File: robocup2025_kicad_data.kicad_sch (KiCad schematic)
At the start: 12 parts, among them U1 RASPBERRY_PI_4B_4GB, U2 ESP32-DEVKITC-32E

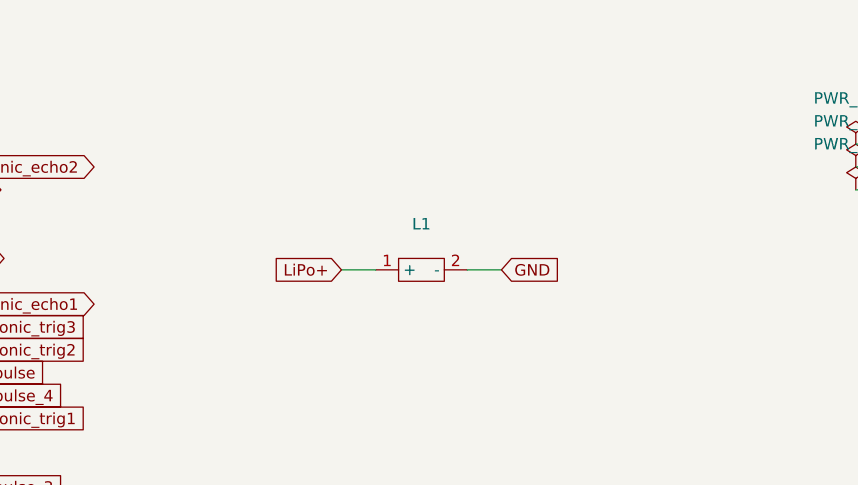
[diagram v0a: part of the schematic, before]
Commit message: robocup2025_kicad_data.kicad_sch: Added voltmeter in schematics
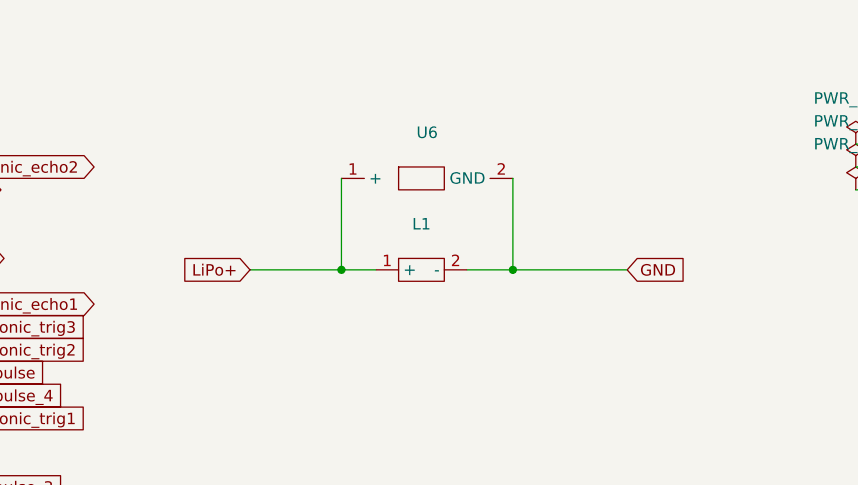
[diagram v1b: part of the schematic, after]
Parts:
- added U6: ~, symbol robo:voltmeter
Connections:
- net GND: now also U6.2 (GND)
- net LiPo+: now also U6.1 (+)
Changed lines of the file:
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@@
 	(generator_version "9.0")
 	(paper "A4")
+	(junction
+		(at 194.31 52.07)
+		(diameter 0)
+		(color 0 0 0 0)
+	)
+	(junction
+		(at 213.36 52.07)
+		(diameter 0)
+		(color 0 0 0 0)
+	)
 	(no_connect
 		(at 80.01 66.04)
@@
 	(wire
 		(pts
+			(xy 213.36 52.07) (xy 226.06 52.07)
+		)
+		(stroke
+			(width 0)
+			(type default)
+		)
+	)
+	(wire
+		(pts
 			(xy 146.05 63.5) (xy 149.86 63.5)
 		)
@@
 	(wire
 		(pts
-			(xy 208.28 52.07) (xy 212.09 52.07)
+			(xy 213.36 41.91) (xy 213.36 52.07)
+		)
+		(stroke
+			(width 0)
+			(type default)
+		)
+	)
+	(wire
+		(pts
+			(xy 208.28 52.07) (xy 213.36 52.07)
 		)
 		(stroke
@@
 	(wire
 		(pts
+			(xy 194.31 41.91) (xy 194.31 52.07)
+		)
+		(stroke
+			(width 0)
+			(type default)
+		)
+	)
+	(wire
+		(pts
+			(xy 184.15 52.07) (xy 194.31 52.07)
+		)
+		(stroke
+			(width 0)
+			(type default)
+		)
+	)
+	(wire
+		(pts
+			(xy 135.89 120.65) (xy 135.89 124.46)
+		)
+		(stroke
+			(width 0)
+			(type default)
+		)
+	)
+	(wire
+		(pts
+			(xy 74.93 121.92) (xy 74.93 125.73)
+		)
+		(stroke
+			(width 0)
+			(type default)
+		)
+	)
+	(wire
+		(pts
+			(xy 146.05 68.58) (xy 149.86 68.58)
+		)
+		(stroke
+			(width 0)
+			(type default)
+		)
+	)
+	(wire
+		(pts
+			(xy 101.6 73.66) (xy 105.41 73.66)
+		)
+		(stroke
+			(width 0)
+			(type default)
+		)
+	)
+	(wire
+		(pts
+			(xy 101.6 58.42) (xy 105.41 58.42)
+		)
+		(stroke
+			(width 0)
+			(type default)
+		)
+	)
+	(wire
+		(pts
+			(xy 146.05 76.2) (xy 149.86 76.2)
+		)
+		(stroke
+			(width 0)
+			(type default)
+		)
+	)
+	(wire
+		(pts
+			(xy 146.05 66.04) (xy 149.86 66.04)
+		)
+		(stroke
+			(width 0)
+			(type default)
+		)
+	)
+	(wire
+		(pts
+			(xy 130.81 120.65) (xy 130.81 124.46)
+		)
+		(stroke
+			(width 0)
+			(type default)
+		)
+	)
+	(wire
+		(pts
 			(xy 194.31 52.07) (xy 198.12 52.07)
 		)
@@
 	(wire
 		(pts
-			(xy 135.89 120.65) (xy 135.89 124.46)
-		)
-		(stroke
-			(width 0)
-			(type default)
-		)
-	)
-	(wire
-		(pts
-			(xy 74.93 121.92) (xy 74.93 125.73)
-		)
-		(stroke
-			(width 0)
-			(type default)
-		)
-	)
-	(wire
-		(pts
-			(xy 146.05 68.58) (xy 149.86 68.58)
-		)
-		(stroke
-			(width 0)
-			(type default)
-		)
-	)
-	(wire
-		(pts
-			(xy 101.6 73.66) (xy 105.41 73.66)
-		)
-		(stroke
-			(width 0)
-			(type default)
-		)
-	)
-	(wire
-		(pts
-			(xy 101.6 58.42) (xy 105.41 58.42)
-		)
-		(stroke
-			(width 0)
-			(type default)
-		)
-	)
-	(wire
-		(pts
-			(xy 146.05 76.2) (xy 149.86 76.2)
-		)
-		(stroke
-			(width 0)
-			(type default)
-		)
-	)
-	(wire
-		(pts
-			(xy 146.05 66.04) (xy 149.86 66.04)
-		)
-		(stroke
-			(width 0)
-			(type default)
-		)
-	)
-	(wire
-		(pts
-			(xy 130.81 120.65) (xy 130.81 124.46)
-		)
-		(stroke
-			(width 0)
-			(type default)
-		)
-	)
-	(wire
-		(pts
 			(xy 132.08 120.65) (xy 132.08 124.46)
 		)
@@
 	(global_label "GND"
 		(shape input)
-		(at 212.09 52.07 0)
+		(at 226.06 52.07 0)
 		(fields_autoplaced yes)
 		(effects
@@
 		)
 		(property "Intersheetrefs" "${INTERSHEET_REFS}"
-			(at 218.9457 52.07 0)
+			(at 232.9157 52.07 0)
 			(effects
 				(font
@@
 	(global_label "LiPo+"
 		(shape input)
-		(at 194.31 52.07 180)
-		(fields_autoplaced yes)
-		(effects
-			(font
-				(size 1.27 1.27)
-			)
-			(justify right)
-		)
-		(property "Intersheetrefs" "${INTERSHEET_REFS}"
-			(at 185.7005 52.07 0)
+		(at 184.15 52.07 180)
+		(fields_autoplaced yes)
+		(effects
+			(font
+				(size 1.27 1.27)
+			)
+			(justify right)
+		)
+		(property "Intersheetrefs" "${INTERSHEET_REFS}"
+			(at 175.5405 52.07 0)
 			(effects
 				(font
@@
 					(unit 1)
 				)
+			)
+		)
+	)
+	(symbol
+		(lib_id "robo:voltmeter")
+		(at 203.2 41.91 0)
+		(unit 1)
+		(exclude_from_sim no)
+		(in_bom yes)
+		(on_board yes)
+		(dnp no)
+		(fields_autoplaced yes)
+		(property "Reference" "U6"
+			(at 203.835 36.83 0)
+			(effects
+				(font
+					(size 1.27 1.27)
+				)
+			)
+		)
+		(property "Value" "~"
+			(at 203.835 39.37 0)
+			(effects
+				(font
+					(size 1.27 1.27)
+				)
+			)
+		)
+		(property "Footprint" ""
+			(at 203.2 41.91 0)
+			(effects
+				(font
+					(size 1.27 1.27)
+				)
+				(hide yes)
+			)
+		)
+		(property "Datasheet" ""
+			(at 203.2 41.91 0)
+			(effects
+				(font
+					(size 1.27 1.27)
+				)
+				(hide yes)
+			)
+		)
+		(property "Description" ""
+			(at 203.2 41.91 0)
+			(effects
+				(font
+					(size 1.27 1.27)
+				)
+				(hide yes)
+			)
+		)
+		(pin "2"
+		)
+		(pin "1"
+		)
+		(instances
+			(project ""
+				(path "/c41ae4e6-c818-4751-9662-d6273ae109e5"
+					(reference "U6")
+					(unit 1)
+				)

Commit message: robocup2025_kicad_data.kicad_sch: Assigned footprint for voltmeter
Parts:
- U6: footprint (none) -> robo:voltmeter
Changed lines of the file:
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@@
 			)
 		)
-		(property "Footprint" ""
+		(property "Footprint" "robo:voltmeter"
 			(at 203.2 41.91 0)
 			(effects

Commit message: robocup2025_kicad_data.kicad_sch: Remaped servo motor's footprints correctly
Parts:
- M1, M2, M3, M4, M5: footprint robo:servo_motor -> robo:servo_motor_4
- M6: footprint (none) -> robo:servo_motor_3
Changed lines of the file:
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@@
 			)
 		)
-		(property "Footprint" "robo:servo_motor"
+		(property "Footprint" "robo:servo_motor_4"
 			(at 54.61 118.11 0)
 			(effects
@@
 			)
 		)
-		(property "Footprint" "robo:servo_motor"
+		(property "Footprint" "robo:servo_motor_4"
 			(at 66.04 118.11 0)
 			(effects
@@
 			)
 		)
-		(property "Footprint" ""
+		(property "Footprint" "robo:servo_motor_3"
 			(at 148.59 120.65 0)
 			(effects
@@
 			)
 		)
-		(property "Footprint" "robo:servo_motor"
+		(property "Footprint" "robo:servo_motor_4"
 			(at 77.47 118.11 0)
 			(effects
@@
 			)
 		)
-		(property "Footprint" "robo:servo_motor"
+		(property "Footprint" "robo:servo_motor_4"
 			(at 88.9 118.11 0)
 			(effects
@@
 			)
 		)
-		(property "Footprint" "robo:servo_motor"
+		(property "Footprint" "robo:servo_motor_4"
 			(at 41.91 118.11 0)
 			(effects

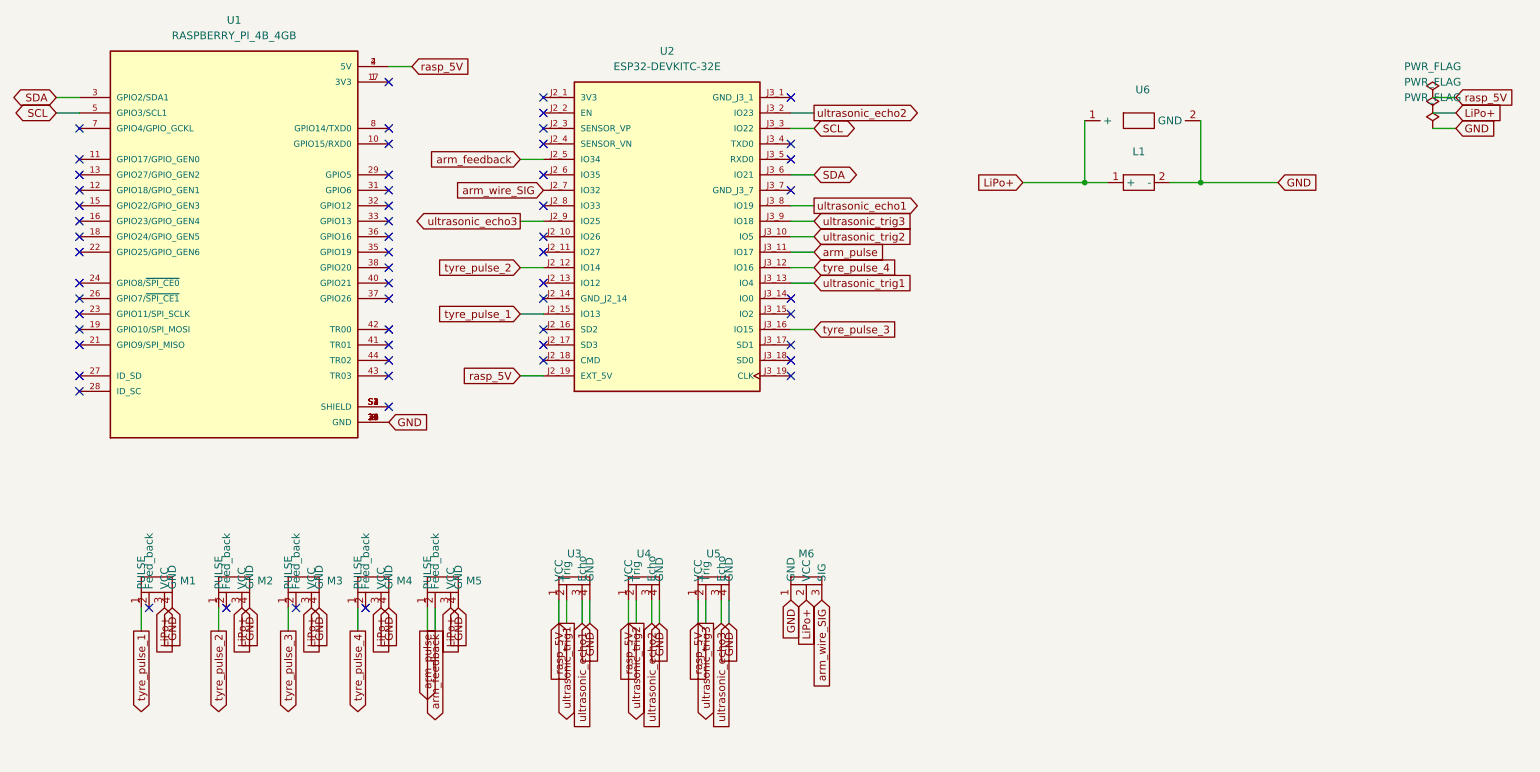
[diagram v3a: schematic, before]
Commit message: robocup2025_kicad_data.kicad_sch: Modified GND to use default symbol
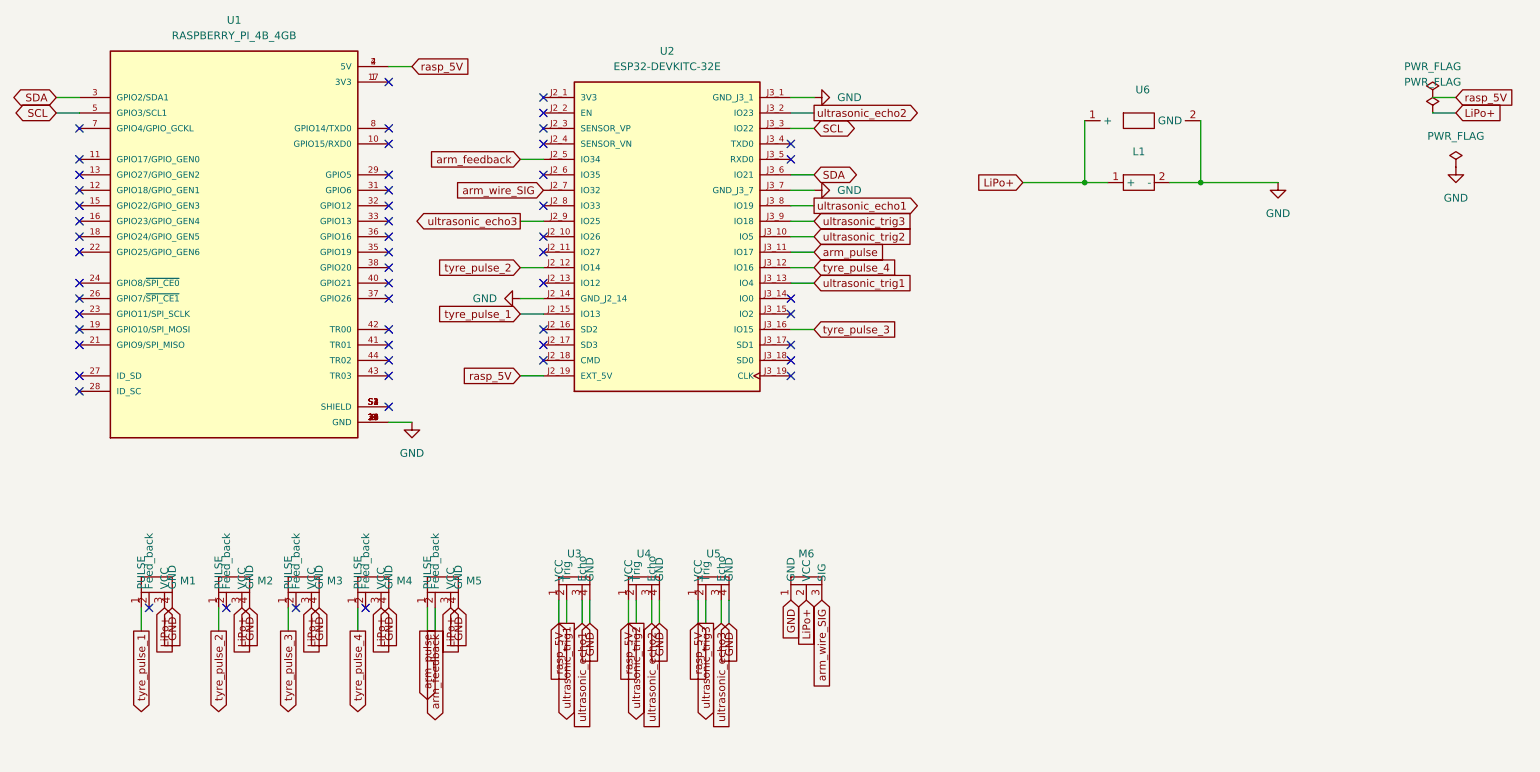
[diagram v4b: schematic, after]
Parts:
- U6: footprint robo:voltmeter -> (none)
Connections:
- net GND: now also U2.J2_14 (GND_J2_14), U2.J3_1 (GND_J3_1), U2.J3_7 (GND_J3_7)
- no-connect marks 58 -> 55

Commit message: robocup2025_kicad_data.kicad_sch: Applied footprint for voltmeter
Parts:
- U6: footprint (none) -> robo:voltmeter
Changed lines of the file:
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@@
 			)
 		)
-		(property "Footprint" ""
+		(property "Footprint" "robo:voltmeter"
 			(at 203.2 41.91 0)
 			(effects

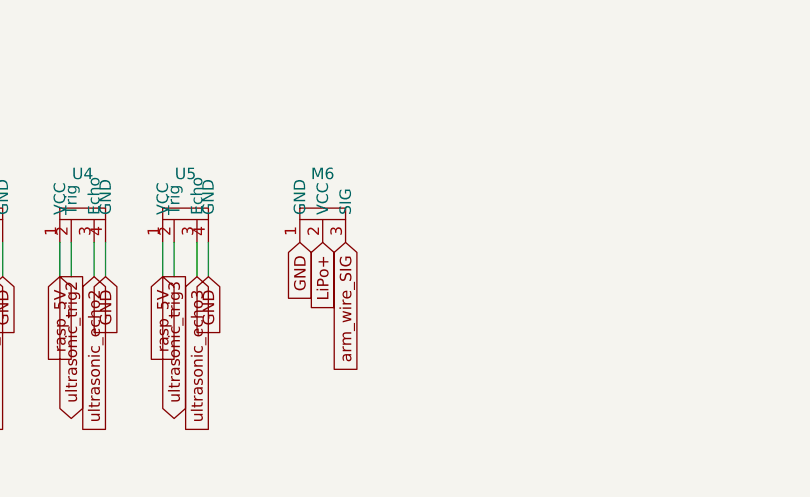
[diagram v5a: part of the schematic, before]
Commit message: robocup2025_kicad_data.kicad_sch: Changed to use default sch for simple servo
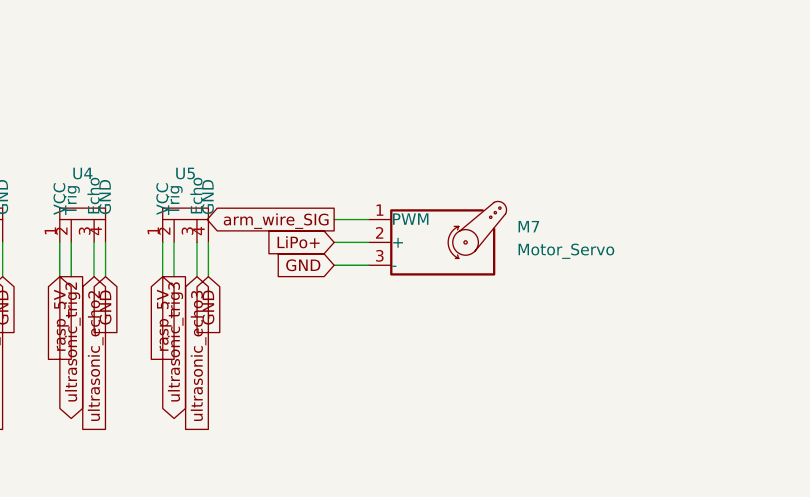
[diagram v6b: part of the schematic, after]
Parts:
- removed M6: ~, robo:servo_motor_3, symbol robo:arm_servo
- added M7: Motor_Servo, symbol Motor:Motor_Servo
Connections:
- net GND: now also M7.3 (-)
- net LiPo+: now also M7.2 (+)
- net arm_wire_SIG: now also M7.1 (PWM)
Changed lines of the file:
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@@
+	(wire
+		(pts
+			(xy 149.86 123.19) (xy 153.67 123.19)
+		)
+		(stroke
+			(width 0)
+			(type default)
+		)
+	)
 	(wire
 		(pts
@@
 	(wire
 		(pts
+			(xy 149.86 118.11) (xy 153.67 118.11)
+		)
+		(stroke
+			(width 0)
+			(type default)
+		)
+	)
+	(wire
+		(pts
 			(xy 194.31 41.91) (xy 194.31 52.07)
 		)
@@
 	(wire
 		(pts
+			(xy 149.86 120.65) (xy 153.67 120.65)
+		)
+		(stroke
+			(width 0)
+			(type default)
+		)
+	)
+	(wire
+		(pts
 			(xy 146.05 66.04) (xy 149.86 66.04)
 		)
@@
 		)
 	)
+	(global_label "LiPo+"
+		(shape input)
+		(at 149.86 120.65 180)
+		(fields_autoplaced yes)
+		(effects
+			(font
+				(size 1.27 1.27)
+			)
+			(justify right)
+		)
+		(property "Intersheetrefs" "${INTERSHEET_REFS}"
+			(at 141.2505 120.65 0)
+			(effects
+				(font
+					(size 1.27 1.27)
+				)
+				(justify right)
+				(hide yes)
+			)
+		)
+	)
 	(global_label "rasp_5V"
 		(shape input)
@@
 		(property "Intersheetrefs" "${INTERSHEET_REFS}"
 			(at 67.31 130.5295 90)
-			(effects
-				(font
-					(size 1.27 1.27)
-				)
-				(justify right)
-				(hide yes)
-			)
-		)
-	)
-	(global_label "LiPo+"
-		(shape input)
-		(at 148.59 120.65 270)
-		(fields_autoplaced yes)
-		(effects
-			(font
-				(size 1.27 1.27)
-			)
-			(justify right)
-		)
-		(property "Intersheetrefs" "${INTERSHEET_REFS}"
-			(at 148.59 129.2595 90)
-			(effects
-				(font
-					(size 1.27 1.27)
-				)
-				(justify right)
-				(hide yes)
-			)
-		)
-	)
-	(global_label "GND"
-		(shape input)
-		(at 146.05 120.65 270)
-		(fields_autoplaced yes)
-		(effects
-			(font
-				(size 1.27 1.27)
-			)
-			(justify right)
-		)
-		(property "Intersheetrefs" "${INTERSHEET_REFS}"
-			(at 146.05 127.5057 90)
 			(effects
 				(font
@@
 		)
 	)
-	(global_label "arm_wire_SIG"
-		(shape input)
-		(at 151.13 120.65 270)
-		(fields_autoplaced yes)
-		(effects
-			(font
-				(size 1.27 1.27)
-			)
-			(justify right)
-		)
-		(property "Intersheetrefs" "${INTERSHEET_REFS}"
-			(at 151.13 136.0933 90)
-			(effects
-				(font
-					(size 1.27 1.27)
-				)
-				(justify right)
-				(hide yes)
-			)
-		)
-	)
 	(global_label "rasp_5V"
 		(shape input)
@@
 		)
 	)
+	(global_label "arm_wire_SIG"
+		(shape output)
+		(at 149.86 118.11 180)
+		(fields_autoplaced yes)
+		(effects
+			(font
+				(size 1.27 1.27)
+			)
+			(justify right)
+		)
+		(property "Intersheetrefs" "${INTERSHEET_REFS}"
+			(at 134.4167 118.11 0)
+			(effects
+				(font
+					(size 1.27 1.27)
+				)
+				(justify right)
+				(hide yes)
+			)
+		)
+	)
 	(global_label "LiPo+"
 		(shape input)
@@
 		(property "Intersheetrefs" "${INTERSHEET_REFS}"
 			(at 134.62 143.5921 90)
+			(effects
+				(font
+					(size 1.27 1.27)
+				)
+				(justify right)
+				(hide yes)
+			)
+		)
+	)
+	(global_label "GND"
+		(shape input)
+		(at 149.86 123.19 180)
+		(fields_autoplaced yes)
+		(effects
+			(font
+				(size 1.27 1.27)
+			)
+			(justify right)
+		)
+		(property "Intersheetrefs" "${INTERSHEET_REFS}"
+			(at 143.0043 123.19 0)
 			(effects
 				(font
@@
 	)
 	(symbol
-		(lib_id "robo:arm_servo")
-		(at 148.59 120.65 0)
-		(unit 1)
-		(exclude_from_sim no)
-		(in_bom yes)
-		(on_board yes)
-		(dnp no)
-		(fields_autoplaced yes)
-		(property "Reference" "M6"
-			(at 148.59 113.03 0)
-			(effects
-				(font
-					(size 1.27 1.27)
-				)
-			)
-		)
-		(property "Value" "~"
-			(at 148.59 115.57 0)
-			(effects
-				(font
-					(size 1.27 1.27)
-				)
-			)
-		)
-		(property "Footprint" "robo:servo_motor_3"
-			(at 148.59 120.65 0)
-			(effects
-				(font
-					(size 1.27 1.27)
-				)
-				(hide yes)
-			)
-		)
-		(property "Datasheet" ""
-			(at 148.59 120.65 0)
-			(effects
-				(font
-					(size 1.27 1.27)
-				)
-				(hide yes)
-			)
-		)
-		(property "Description" ""
-			(at 148.59 120.65 0)
-			(effects
-				(font
-					(size 1.27 1.27)
-				)
-				(hide yes)
-			)
-		)
-		(pin "2"
-		)
-		(pin "1"
-		)
-		(pin "3"
-		)
-		(instances
-			(project ""
-				(path "/c41ae4e6-c818-4751-9662-d6273ae109e5"
-					(reference "M6")
-					(unit 1)
-				)
-			)
-		)
-	)
-	(symbol
 		(lib_id "robo:servo_motor")
 		(at 77.47 118.11 0)
@@
 					(unit 1)
 				)
+			)
+		)
+	)
+	(symbol
+		(lib_id "Motor:Motor_Servo")
+		(at 161.29 120.65 0)
+		(unit 1)
+		(exclude_from_sim no)
+		(in_bom yes)
+		(on_board yes)
+		(dnp no)
+		(fields_autoplaced yes)
+		(property "Reference" "M7"
+			(at 170.18 118.9468 0)
+			(effects
+				(font
+					(size 1.27 1.27)
+				)
+				(justify left)
+			)
+		)
+		(property "Value" "Motor_Servo"
+			(at 170.18 121.4868 0)
+			(effects
+				(font
+					(size 1.27 1.27)
+				)
+				(justify left)
+			)
+		)
+		(property "Footprint" ""
+			(at 161.29 125.476 0)
+			(effects
+				(font
+					(size 1.27 1.27)
+				)
+				(hide yes)
+			)
+		)
+		(property "Datasheet" "http://forums.parallax.com/uploads/attachments/46831/74481.png"
+			(at 161.29 125.476 0)
+			(effects
+				(font
+					(size 1.27 1.27)
+				)
+				(hide yes)
+			)
+		)
+		(property "Description" "Servo Motor (Futaba, HiTec, JR connector)"
+			(at 161.29 120.65 0)
+			(effects
+				(font
+					(size 1.27 1.27)
+				)
+				(hide yes)
+			)
+		)
+		(pin "3"
+		)
+		(pin "2"
+		)
+		(pin "1"
+		)
+		(instances
+			(project "robocup2025_kicad_data"
+				(path "/c41ae4e6-c818-4751-9662-d6273ae109e5"
+					(reference "M7")
+					(unit 1)
+				)

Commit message: auto_saved_files#,_autosave-robocup2025_kicad_data.kicad_sch robocup2025_kicad_data.kicad_sch: Assigned footprint for simple servo motor
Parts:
- M7: footprint (none) -> robo:servo_motor_3
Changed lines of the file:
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@@
 			)
 		)
-		(property "Footprint" ""
+		(property "Footprint" "robo:servo_motor_3"
 			(at 161.29 125.476 0)
 			(effects
